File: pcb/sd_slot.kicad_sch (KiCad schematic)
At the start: 4 parts, among them J7 MICROSD

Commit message: Still tidying pcb design
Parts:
- C8: footprint Capacitor_SMD:C_01005_0402Metric -> Capacitor_SMD:C_0402_1005Metric
- R11, R12: footprint Resistor_SMD:R_0201_0603Metric -> Resistor_SMD:R_0603_1608Metric
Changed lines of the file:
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@@
 			)
 		)
-		(property "Footprint" "Resistor_SMD:R_0201_0603Metric"
+		(property "Footprint" "Resistor_SMD:R_0603_1608Metric"
 			(at 133.35 90.678 90)
 			(hide yes)
@@
 			)
 		)
-		(property "Footprint" "Capacitor_SMD:C_01005_0402Metric"
+		(property "Footprint" "Capacitor_SMD:C_0402_1005Metric"
 			(at 100.6348 77.47 0)
 			(hide yes)
@@
 			)
 		)
-		(property "Footprint" "Resistor_SMD:R_0201_0603Metric"
+		(property "Footprint" "Resistor_SMD:R_0603_1608Metric"
 			(at 133.35 71.628 90)
 			(hide yes)

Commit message: Still improving pcb, I learned what a fiducial is today
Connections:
- net 3V renamed +3.3V
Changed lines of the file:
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@@
-		)
-	)
-	(hierarchical_label "3V"
-		(shape input)
-		(at 97.79 77.47 180)
-		(effects
-			(font
-				(size 1.27 1.27)
-			)
-			(justify right)
 		)
 	)
@@
 		(shape input)
 		(at 123.19 74.93 180)
-		(effects
-			(font
-				(size 1.27 1.27)
-			)
-			(justify right)
-		)
-	)
-	(hierarchical_label "GND"
-		(shape input)
-		(at 97.79 85.09 180)
 		(effects
 			(font
@@
 	)
 	(symbol
+		(lib_id "power:GND")
+		(at 97.79 85.09 270)
+		(unit 1)
+		(body_style 1)
+		(exclude_from_sim no)
+		(in_bom yes)
+		(on_board yes)
+		(in_pos_files yes)
+		(dnp no)
+		(fields_autoplaced yes)
+		(property "Reference" "#PWR015"
+			(at 91.44 85.09 0)
+			(hide yes)
+			(show_name no)
+			(do_not_autoplace no)
+			(effects
+				(font
+					(size 1.27 1.27)
+				)
+			)
+		)
+		(property "Value" "GND"
+			(at 93.98 85.0899 90)
+			(show_name no)
+			(do_not_autoplace no)
+			(effects
+				(font
+					(size 1.27 1.27)
+				)
+				(justify right)
+			)
+		)
+		(property "Footprint" ""
+			(at 97.79 85.09 0)
+			(hide yes)
+			(show_name no)
+			(do_not_autoplace no)
+			(effects
+				(font
+					(size 1.27 1.27)
+				)
+			)
+		)
+		(property "Datasheet" ""
+			(at 97.79 85.09 0)
+			(hide yes)
+			(show_name no)
+			(do_not_autoplace no)
+			(effects
+				(font
+					(size 1.27 1.27)
+				)
+			)
+		)
+		(property "Description" "Power symbol creates a global label with name \"GND\" , ground"
+			(at 97.79 85.09 0)
+			(hide yes)
+			(show_name no)
+			(do_not_autoplace no)
+			(effects
+				(font
+					(size 1.27 1.27)
+				)
+			)
+		)
+		(pin "1"
+		)
+		(instances
+			(project "packmate"
+				(path "/1b0954a2-3127-4772-a3bb-573d547242ae/0e612a4d-fbe2-4c32-bbe2-8603c0e18762"
+					(reference "#PWR015")
+					(unit 1)
+				)
+			)
+		)
+	)
+	(symbol
 		(lib_id "Device:R")
 		(at 133.35 88.9 90)
@@
 					(unit 1)
 				)
+			)
+		)
+	)
+	(symbol
+		(lib_id "power:+3.3V")
+		(at 97.79 77.47 90)
+		(unit 1)
+		(body_style 1)
+		(exclude_from_sim no)
+		(in_bom yes)
+		(on_board yes)
+		(in_pos_files yes)
+		(dnp no)
+		(fields_autoplaced yes)
+		(property "Reference" "#PWR026"
+			(at 101.6 77.47 0)
+			(hide yes)
+			(show_name no)
+			(do_not_autoplace no)
+			(effects
+				(font
+					(size 1.27 1.27)
+				)
+			)
+		)
+		(property "Value" "+3.3V"
+			(at 93.98 77.4699 90)
+			(show_name no)
+			(do_not_autoplace no)
+			(effects
+				(font
+					(size 1.27 1.27)
+				)
+				(justify left)
+			)
+		)
+		(property "Footprint" ""
+			(at 97.79 77.47 0)
+			(hide yes)
+			(show_name no)
+			(do_not_autoplace no)
+			(effects
+				(font
+					(size 1.27 1.27)
+				)
+			)
+		)
+		(property "Datasheet" ""
+			(at 97.79 77.47 0)
+			(hide yes)
+			(show_name no)
+			(do_not_autoplace no)
+			(effects
+				(font
+					(size 1.27 1.27)
+				)
+			)
+		)
+		(property "Description" "Power symbol creates a global label with name \"+3.3V\""
+			(at 97.79 77.47 0)
+			(hide yes)
+			(show_name no)
+			(do_not_autoplace no)
+			(effects
+				(font
+					(size 1.27 1.27)
+				)
+			)
+		)
+		(pin "1"
+		)
+		(instances
+			(project "packmate"
+				(path "/1b0954a2-3127-4772-a3bb-573d547242ae/0e612a4d-fbe2-4c32-bbe2-8603c0e18762"
+					(reference "#PWR026")
+					(unit 1)
+				)

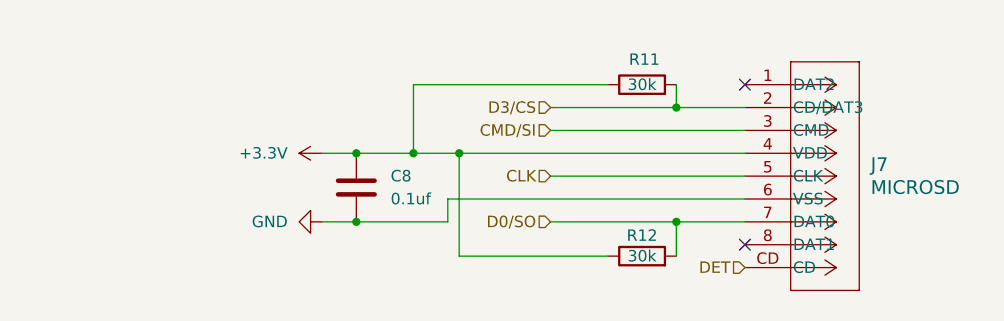
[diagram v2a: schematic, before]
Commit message: I think the PCB is almost done for real this time chat. Just gotta add part numbers for the BOM
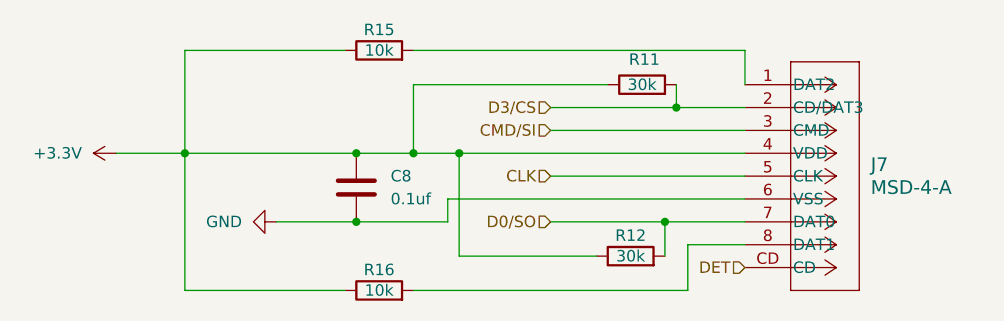
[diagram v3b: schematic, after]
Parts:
- added R15, R16: 10k, Resistor_SMD:R_0603_1608Metric, symbol Device:R
- J7: value MICROSD -> MSD-4-A
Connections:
- net +3.3V: now also R15.1, R16.1
- net at J7.1 (DAT2): now also R15.2
- net at J7.8 (DAT1): now also R16.2
- no-connect marks 2 -> 0
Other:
- moved on the sheet: R12

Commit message: I think the PCB is ready to ship, just gonna tidy up a couple more things
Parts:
- C8: MPN (none) -> GRM155R71H104KE14D; Manufacturer (none) -> Murata Electronics
- J7: MPN (none) -> MSD-4-A; Manufacturer (none) -> Same Sky (Formerly CUI Devices); SilkLabel (none) -> MICROSD
- R11, R12: MPN (none) -> RC0603FR-0730KL; Manufacturer (none) -> Yageo
- R15, R16: MPN (none) -> CRCW060310K0FKEA; Manufacturer (none) -> Vishay Dale
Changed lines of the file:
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@@
+			)
+		)
+		(property "MPN" "MSD-4-A"
+			(at 144.78 69.85 0)
+			(hide yes)
+			(show_name no)
+			(do_not_autoplace no)
+			(effects
+				(font
+					(size 1.27 1.27)
+				)
+			)
+		)
+		(property "Manufacturer" "Same Sky (Formerly CUI Devices)"
+			(at 144.78 69.85 0)
+			(hide yes)
+			(show_name no)
+			(do_not_autoplace no)
+			(effects
+				(font
+					(size 1.27 1.27)
+				)
+			)
+		)
+		(property "SilkLabel" "MICROSD"
+			(at 144.78 69.85 0)
+			(hide yes)
+			(show_name no)
+			(do_not_autoplace no)
+			(effects
+				(font
+					(size 1.27 1.27)
+				)
 			)
 		)
@@
 		)
 		(property "Sim.Type" ""
+			(at 104.14 66.04 90)
+			(hide yes)
+			(show_name no)
+			(do_not_autoplace no)
+			(effects
+				(font
+					(size 1.27 1.27)
+				)
+			)
+		)
+		(property "MPN" "CRCW060310K0FKEA"
+			(at 104.14 66.04 90)
+			(hide yes)
+			(show_name no)
+			(do_not_autoplace no)
+			(effects
+				(font
+					(size 1.27 1.27)
+				)
+			)
+		)
+		(property "Manufacturer" "Vishay Dale"
+			(at 104.14 66.04 90)
+			(hide yes)
+			(show_name no)
+			(do_not_autoplace no)
+			(effects
+				(font
+					(size 1.27 1.27)
+				)
+			)
+		)
+		(property "SilkLabel" ""
 			(at 104.14 66.04 90)
 			(hide yes)
@@
 			)
 		)
+		(property "MPN" "CRCW060310K0FKEA"
+			(at 104.14 92.71 90)
+			(hide yes)
+			(show_name no)
+			(do_not_autoplace no)
+			(effects
+				(font
+					(size 1.27 1.27)
+				)
+			)
+		)
+		(property "Manufacturer" "Vishay Dale"
+			(at 104.14 92.71 90)
+			(hide yes)
+			(show_name no)
+			(do_not_autoplace no)
+			(effects
+				(font
+					(size 1.27 1.27)
+				)
+			)
+		)
+		(property "SilkLabel" ""
+			(at 104.14 92.71 90)
+			(hide yes)
+			(show_name no)
+			(do_not_autoplace no)
+			(effects
+				(font
+					(size 1.27 1.27)
+				)
+			)
+		)
 		(pin "2"
 		)
@@
 		)
 		(property "Sim.Type" ""
+			(at 132.08 88.9 90)
+			(hide yes)
+			(show_name no)
+			(do_not_autoplace no)
+			(effects
+				(font
+					(size 1.27 1.27)
+				)
+			)
+		)
+		(property "MPN" "RC0603FR-0730KL"
+			(at 132.08 88.9 90)
+			(hide yes)
+			(show_name no)
+			(do_not_autoplace no)
+			(effects
+				(font
+					(size 1.27 1.27)
+				)
+			)
+		)
+		(property "Manufacturer" "Yageo"
+			(at 132.08 88.9 90)
+			(hide yes)
+			(show_name no)
+			(do_not_autoplace no)
+			(effects
+				(font
+					(size 1.27 1.27)
+				)
+			)
+		)
+		(property "SilkLabel" ""
 			(at 132.08 88.9 90)
 			(hide yes)
@@
 			)
 		)
+		(property "MPN" "GRM155R71H104KE14D"
+			(at 101.6 81.28 0)
+			(hide yes)
+			(show_name no)
+			(do_not_autoplace no)
+			(effects
+				(font
+					(size 1.27 1.27)
+				)
+			)
+		)
+		(property "Manufacturer" "Murata Electronics"
+			(at 101.6 81.28 0)
+			(hide yes)
+			(show_name no)
+			(do_not_autoplace no)
+			(effects
+				(font
+					(size 1.27 1.27)
+				)
+			)
+		)
+		(property "SilkLabel" ""
+			(at 101.6 81.28 0)
+			(hide yes)
+			(show_name no)
+			(do_not_autoplace no)
+			(effects
+				(font
+					(size 1.27 1.27)
+				)
+			)
+		)
 		(pin "2"
 		)
@@
 			(at 133.35 69.85 90)
 			(hide yes)
+			(show_name no)
+			(do_not_autoplace no)
+			(effects
+				(font
+					(size 1.27 1.27)
+				)
+			)
+		)
+		(property "MPN" "RC0603FR-0730KL"
+			(at 133.35 69.85 90)
+			(hide yes)
+			(show_name no)
+			(do_not_autoplace no)
+			(effects
+				(font
+					(size 1.27 1.27)
+				)
+			)
+		)
+		(property "Manufacturer" "Yageo"
+			(at 133.35 69.85 90)
+			(hide yes)
+			(show_name no)
+			(do_not_autoplace no)
+			(effects
+				(font
+					(size 1.27 1.27)
+				)
+			)
+		)
+		(property "SilkLabel" ""
+			(at 133.35 69.85 90)
+			(hide yes)
